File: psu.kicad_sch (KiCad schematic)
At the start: 25 parts, among them J2801 Barrel_Jack_Switch, U2801 L78L05_SOT89, U2802 TL972

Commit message: PSU schem update
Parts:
- C2805: value 10n -> 22u
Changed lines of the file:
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@@
   (junction (at 50.8 149.86) (diameter 0) (color 0 0 0 0)
   )
-  (junction (at 63.5 58.42) (diameter 0) (color 0 0 0 0)
+  (junction (at 27.94 100.33) (diameter 0) (color 0 0 0 0)
   )
   (no_connect (at 39.37 31.75))
@@
     (stroke (width 0) (type default) (color 0 0 0 0))
   )
+  (wire (pts (xy 27.94 100.33) (xy 27.94 105.41))
+    (stroke (width 0) (type default) (color 0 0 0 0))
+  )
   (wire (pts (xy 167.64 97.79) (xy 167.64 100.33))
     (stroke (width 0) (type default) (color 0 0 0 0))
@@
     (stroke (width 0) (type default) (color 0 0 0 0))
   )
-  (wire (pts (xy 27.305 100.33) (xy 31.75 100.33))
+  (wire (pts (xy 21.59 100.33) (xy 27.94 100.33))
     (stroke (width 0) (type default) (color 0 0 0 0))
   )
@@
     (stroke (width 0) (type default) (color 0 0 0 0))
   )
-  (wire (pts (xy 63.5 58.42) (xy 63.5 63.5))
-    (stroke (width 0) (type default) (color 0 0 0 0))
-  )
   (wire (pts (xy 135.89 121.92) (xy 151.13 121.92))
     (stroke (width 0) (type default) (color 0 0 0 0))
@@
     (stroke (width 0) (type default) (color 0 0 0 0))
   )
-  (wire (pts (xy 63.5 58.42) (xy 68.58 58.42))
-    (stroke (width 0) (type default) (color 0 0 0 0))
-  )
   (wire (pts (xy 66.04 100.33) (xy 66.04 105.41))
     (stroke (width 0) (type default) (color 0 0 0 0))
@@
     (stroke (width 0) (type default) (color 0 0 0 0))
   )
+  (wire (pts (xy 27.94 113.03) (xy 27.94 115.57))
+    (stroke (width 0) (type default) (color 0 0 0 0))
+  )
   (wire (pts (xy 43.18 29.21) (xy 43.18 25.4))
     (stroke (width 0) (type default) (color 0 0 0 0))
@@
     (stroke (width 0) (type default) (color 0 0 0 0))
   )
+  (wire (pts (xy 27.94 100.33) (xy 31.75 100.33))
+    (stroke (width 0) (type default) (color 0 0 0 0))
+  )
   (wire (pts (xy 109.22 138.43) (xy 125.73 138.43))
     (stroke (width 0) (type default) (color 0 0 0 0))
@@
     (stroke (width 0) (type default) (color 0 0 0 0))
   )
-  (wire (pts (xy 63.5 71.12) (xy 63.5 73.66))
-    (stroke (width 0) (type default) (color 0 0 0 0))
-  )
-  (wire (pts (xy 45.72 58.42) (xy 63.5 58.42))
+  (wire (pts (xy 45.72 58.42) (xy 68.58 58.42))
     (stroke (width 0) (type default) (color 0 0 0 0))
   )
@@
     (effects (font (size 1.27 1.27)) (justify right))
   )
-  (hierarchical_label "GND" (shape input) (at 63.5 73.66 270)
-    (effects (font (size 1.27 1.27)) (justify right))
-  )
   (hierarchical_label "+5V" (shape output) (at 69.85 138.43 0)
     (effects (font (size 1.27 1.27)) (justify left))
@@
     (effects (font (size 1.27 1.27)) (justify left))
   )
+  (hierarchical_label "GND" (shape input) (at 27.94 115.57 270)
+    (effects (font (size 1.27 1.27)) (justify right))
+  )
   (hierarchical_label "GND" (shape output) (at 190.5 111.76 270)
     (effects (font (size 1.27 1.27)) (justify right))
   )
-  (hierarchical_label "+9Vd" (shape output) (at 27.305 100.33 180)
-    (effects (font (size 1.27 1.27)) (justify right))
-  )
-  (symbol (lib_id "Device:C_Polarized") (at 63.5 67.31 0) (unit 1)
-    (in_bom yes) (on_board yes)
-    (property "Reference" "C2805" (id 0) (at 60.5028 68.4784 0)
-      (effects (font (size 1.27 1.27)) (justify right))
-    )
-    (property "Value" "10n" (id 1) (at 60.5028 66.167 0)
-      (effects (font (size 1.27 1.27)) (justify right))
-    )
-    (property "Footprint" "Capacitor_SMD:CP_Elec_6.3x5.3" (id 2) (at 64.4652 71.12 0)
-      (effects (font (size 1.27 1.27)) hide)
-    )
-    (property "Datasheet" "~" (id 3) (at 63.5 67.31 0)
-      (effects (font (size 1.27 1.27)) hide)
-    )
-    (property "LCSC" "C176674" (id 4) (at 63.5 67.31 0)
-      (effects (font (size 1.27 1.27)) hide)
-    )
-    (pin "1")
-    (pin "2")
+  (hierarchical_label "+9Vd" (shape output) (at 21.59 100.33 180)
+    (effects (font (size 1.27 1.27)) (justify right))
   )
   (symbol (lib_id "Device:Polyfuse") (at 35.56 58.42 90) (unit 1)
@@
     (pin "8")
   )
+  (symbol (lib_id "Device:C_Polarized") (at 27.94 109.22 0) (unit 1)
+    (in_bom yes) (on_board yes)
+    (property "Reference" "C2805" (id 0) (at 24.9428 110.3884 0)
+      (effects (font (size 1.27 1.27)) (justify right))
+    )
+    (property "Value" "22u" (id 1) (at 24.9428 108.077 0)
+      (effects (font (size 1.27 1.27)) (justify right))
+    )
+    (property "Footprint" "Capacitor_SMD:CP_Elec_6.3x5.3" (id 2) (at 28.9052 113.03 0)
+      (effects (font (size 1.27 1.27)) hide)
+    )
+    (property "Datasheet" "~" (id 3) (at 27.94 109.22 0)
+      (effects (font (size 1.27 1.27)) hide)
+    )
+    (property "LCSC" "C176674" (id 4) (at 27.94 109.22 0)
+      (effects (font (size 1.27 1.27)) hide)
+    )
+    (pin "1")
+    (pin "2")
+  )
   (symbol (lib_id "Device:C_Polarized") (at 66.04 109.22 0) (unit 1)

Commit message: Mixer redesign wip
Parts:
- added J2802: Conn_02x04_Counter_Clockwise, Connector_PinSocket_2.54mm:PinSocket_2x04_P2.54mm_Vertical, symbol Connector_Generic:Conn_02x04_Odd_Even
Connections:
- net +4.5V: now also J2802.3 (Pin_3), J2802.4 (Pin_4)
- net +5V: now also J2802.5 (Pin_5), J2802.6 (Pin_6)
- net +9Va: now also J2802.1 (Pin_1), J2802.2 (Pin_2)
- net GND: now also J2802.7 (Pin_7), J2802.8 (Pin_8)
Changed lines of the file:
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@@
+    (stroke (width 0) (type default) (color 0 0 0 0))
+  )
+  (wire (pts (xy 132.715 31.75) (xy 137.795 31.75))
     (stroke (width 0) (type default) (color 0 0 0 0))
   )
@@
     (stroke (width 0) (type default) (color 0 0 0 0))
   )
+  (wire (pts (xy 132.715 36.83) (xy 137.795 36.83))
+    (stroke (width 0) (type default) (color 0 0 0 0))
+  )
   (wire (pts (xy 179.07 146.05) (xy 179.07 149.86))
     (stroke (width 0) (type default) (color 0 0 0 0))
   )
+  (wire (pts (xy 150.495 36.83) (xy 156.21 36.83))
+    (stroke (width 0) (type default) (color 0 0 0 0))
+  )
   (wire (pts (xy 54.61 113.03) (xy 54.61 115.57))
     (stroke (width 0) (type default) (color 0 0 0 0))
@@
     (stroke (width 0) (type default) (color 0 0 0 0))
   )
+  (wire (pts (xy 150.495 29.21) (xy 156.21 29.21))
+    (stroke (width 0) (type default) (color 0 0 0 0))
+  )
   (wire (pts (xy 167.64 107.95) (xy 167.64 111.76))
     (stroke (width 0) (type default) (color 0 0 0 0))
@@
     (stroke (width 0) (type default) (color 0 0 0 0))
   )
+  (wire (pts (xy 150.495 31.75) (xy 156.21 31.75))
+    (stroke (width 0) (type default) (color 0 0 0 0))
+  )
   (wire (pts (xy 161.29 135.89) (xy 179.07 135.89))
     (stroke (width 0) (type default) (color 0 0 0 0))
   )
+  (wire (pts (xy 150.495 34.29) (xy 156.21 34.29))
+    (stroke (width 0) (type default) (color 0 0 0 0))
+  )
   (wire (pts (xy 60.96 138.43) (xy 69.85 138.43))
     (stroke (width 0) (type default) (color 0 0 0 0))
@@
     (stroke (width 0) (type default) (color 0 0 0 0))
   )
+  (wire (pts (xy 132.715 34.29) (xy 137.795 34.29))
+    (stroke (width 0) (type default) (color 0 0 0 0))
+  )
   (wire (pts (xy 109.22 140.97) (xy 109.22 138.43))
     (stroke (width 0) (type default) (color 0 0 0 0))
@@
   )
   (wire (pts (xy 109.22 138.43) (xy 125.73 138.43))
+    (stroke (width 0) (type default) (color 0 0 0 0))
+  )
+  (wire (pts (xy 132.715 29.21) (xy 137.795 29.21))
     (stroke (width 0) (type default) (color 0 0 0 0))
   )
@@
     (effects (font (size 1.27 1.27)) (justify right))
   )
+  (hierarchical_label "+5V" (shape output) (at 156.21 34.29 0)
+    (effects (font (size 1.27 1.27)) (justify left))
+  )
+  (hierarchical_label "GND" (shape output) (at 156.21 36.83 0)
+    (effects (font (size 1.27 1.27)) (justify left))
+  )
+  (hierarchical_label "+9Va" (shape output) (at 132.715 29.21 180)
+    (effects (font (size 1.27 1.27)) (justify right))
+  )
   (hierarchical_label "GND" (shape output) (at 259.08 50.8 270)
     (effects (font (size 1.27 1.27)) (justify right))
@@
     (effects (font (size 1.27 1.27)) (justify left))
   )
+  (hierarchical_label "+5V" (shape output) (at 132.715 34.29 180)
+    (effects (font (size 1.27 1.27)) (justify right))
+  )
   (hierarchical_label "GND" (shape output) (at 109.22 149.86 270)
     (effects (font (size 1.27 1.27)) (justify right))
   )
-  (hierarchical_label "GND" (shape input) (at 43.18 115.57 270)
+  (hierarchical_label "GND" (shape output) (at 43.18 115.57 270)
     (effects (font (size 1.27 1.27)) (justify right))
   )
@@
     (effects (font (size 1.27 1.27)) (justify right))
   )
-  (hierarchical_label "GND" (shape input) (at 50.8 151.13 270)
-    (effects (font (size 1.27 1.27)) (justify right))
-  )
-  (hierarchical_label "GND" (shape input) (at 45.72 73.66 270)
-    (effects (font (size 1.27 1.27)) (justify right))
+  (hierarchical_label "GND" (shape output) (at 50.8 151.13 270)
+    (effects (font (size 1.27 1.27)) (justify right))
+  )
+  (hierarchical_label "GND" (shape output) (at 45.72 73.66 270)
+    (effects (font (size 1.27 1.27)) (justify right))
+  )
+  (hierarchical_label "+9Va" (shape output) (at 156.21 29.21 0)
+    (effects (font (size 1.27 1.27)) (justify left))
+  )
+  (hierarchical_label "+4.5V" (shape output) (at 156.21 31.75 0)
+    (effects (font (size 1.27 1.27)) (justify left))
   )
   (hierarchical_label "+9Va" (shape output) (at 109.22 88.9 90)
     (effects (font (size 1.27 1.27)) (justify left))
   )
-  (hierarchical_label "GND" (shape input) (at 66.04 115.57 270)
-    (effects (font (size 1.27 1.27)) (justify right))
-  )
-  (hierarchical_label "GND" (shape input) (at 54.61 115.57 270)
+  (hierarchical_label "GND" (shape output) (at 66.04 115.57 270)
+    (effects (font (size 1.27 1.27)) (justify right))
+  )
+  (hierarchical_label "GND" (shape output) (at 54.61 115.57 270)
+    (effects (font (size 1.27 1.27)) (justify right))
+  )
+  (hierarchical_label "GND" (shape output) (at 132.715 36.83 180)
     (effects (font (size 1.27 1.27)) (justify right))
   )
@@
     (effects (font (size 1.27 1.27)) (justify right))
   )
+  (hierarchical_label "+4.5V" (shape output) (at 132.715 31.75 180)
+    (effects (font (size 1.27 1.27)) (justify right))
+  )
   (hierarchical_label "GND" (shape output) (at 167.64 111.76 270)
     (effects (font (size 1.27 1.27)) (justify right))
@@
     (effects (font (size 1.27 1.27)) (justify left))
   )
-  (hierarchical_label "GND" (shape input) (at 27.94 115.57 270)
+  (hierarchical_label "GND" (shape output) (at 27.94 115.57 270)
     (effects (font (size 1.27 1.27)) (justify right))
   )
@@
     (pin "2")
   )
+  (symbol (lib_id "Connector_Generic:Conn_02x04_Odd_Even") (at 142.875 31.75 0) (unit 1)
+    (in_bom yes) (on_board yes) (fields_autoplaced)
+    (property "Reference" "J2802" (id 0) (at 144.145 22.86 0))
+    (property "Value" "Conn_02x04_Counter_Clockwise" (id 1) (at 144.145 25.4 0))
+    (property "Footprint" "Connector_PinSocket_2.54mm:PinSocket_2x04_P2.54mm_Vertical" (id 2) (at 142.875 31.75 0)
+      (effects (font (size 1.27 1.27)) hide)
+    )
+    (property "Datasheet" "~" (id 3) (at 142.875 31.75 0)
+      (effects (font (size 1.27 1.27)) hide)
+    )
+    (pin "1")
+    (pin "2")
+    (pin "3")
+    (pin "4")
+    (pin "5")
+    (pin "6")
+    (pin "7")
+    (pin "8")
+  )
   (symbol (lib_id "Device:C_Polarized") (at 54.61 109.22 0) (unit 1)

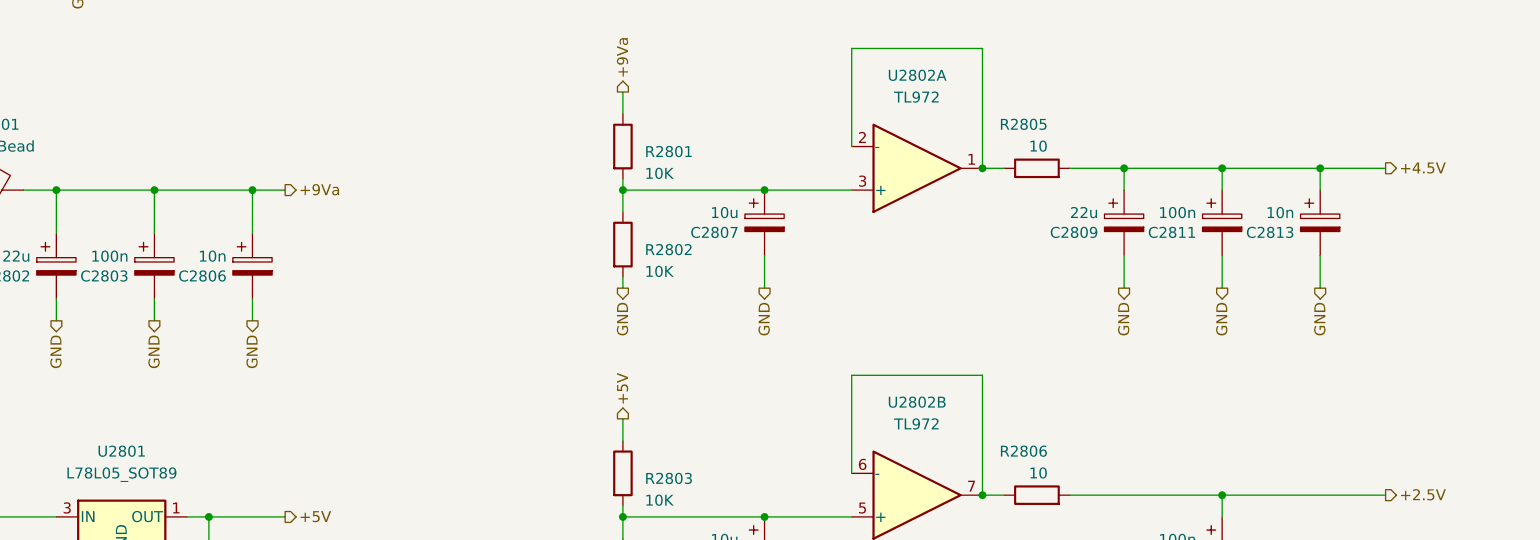
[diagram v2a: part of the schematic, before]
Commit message: Add JLC parts numbers
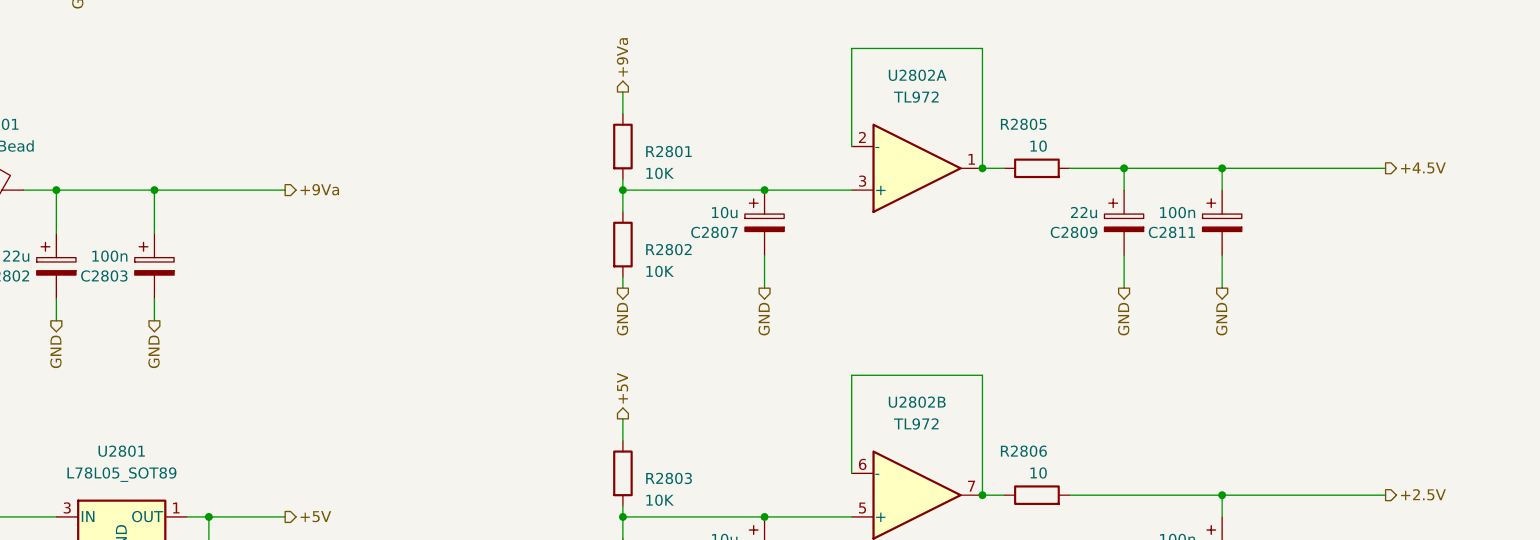
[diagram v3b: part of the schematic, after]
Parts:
- removed C2806, C2813: 10n, Capacitor_SMD:CP_Elec_6.3x5.3, symbol Device:C_Polarized
- C2801: LCSC (none) -> C264238; Role (none) -> psu-filter
- C2802, C2805, C2809: footprint Capacitor_SMD:CP_Elec_6.3x5.3 -> Capacitor_SMD:CP_Elec_4x5.4; LCSC C176674 -> C98746; Role (none) -> psu-filter
- C2803, C2811, C2812: footprint Capacitor_SMD:CP_Elec_6.3x5.3 -> Capacitor_SMD:CP_Elec_4x5.4; LCSC C176674 -> C271438; Role (none) -> psu-filter
- C2804: LCSC (none) -> C271438; Role (none) -> psu-filter
- C2807, C2808: footprint Capacitor_SMD:CP_Elec_6.3x5.3 -> Capacitor_SMD:CP_Elec_4x5.4; LCSC C176674 -> C294524; Role (none) -> psu-filter
- C2815: LCSC (none) -> C497032; Role (none) -> ic-bypass
- D2801: LCSC (none) -> C122841
- FB2801: LCSC (none) -> C155088
- R2801, R2802, R2803, R2804: LCSC (none) -> C98220
- R2805, R2806: LCSC (none) -> C323549
- U2801: LCSC (none) -> C347258
- U2802: LCSC (none) -> C46127
